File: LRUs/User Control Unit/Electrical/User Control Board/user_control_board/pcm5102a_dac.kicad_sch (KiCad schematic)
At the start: 1 part, among them U2 PCM5102A

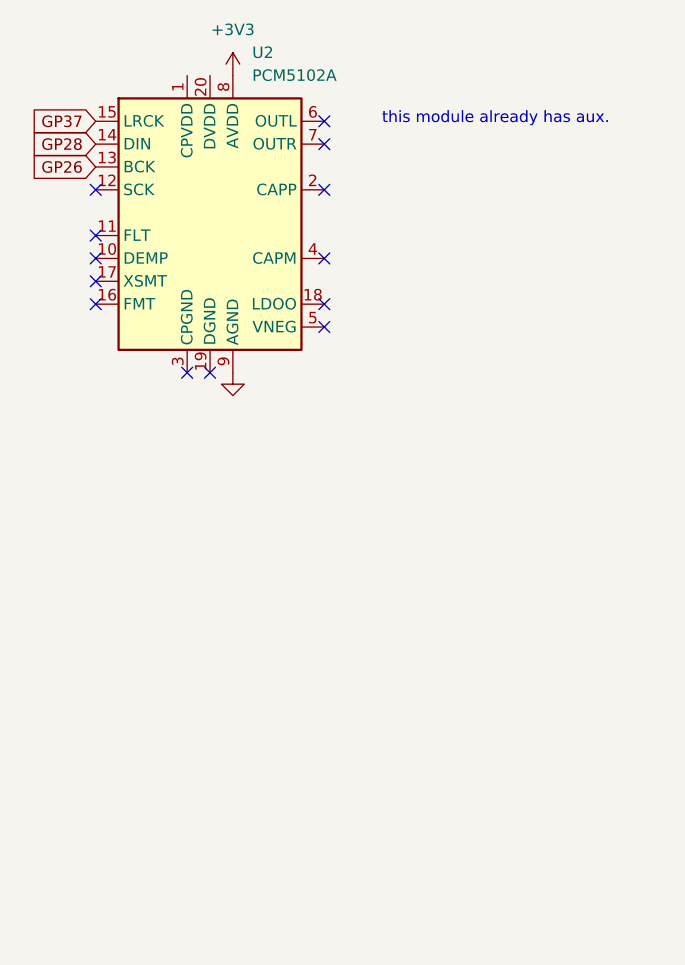
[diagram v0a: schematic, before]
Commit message: footprint and added symbol for audio
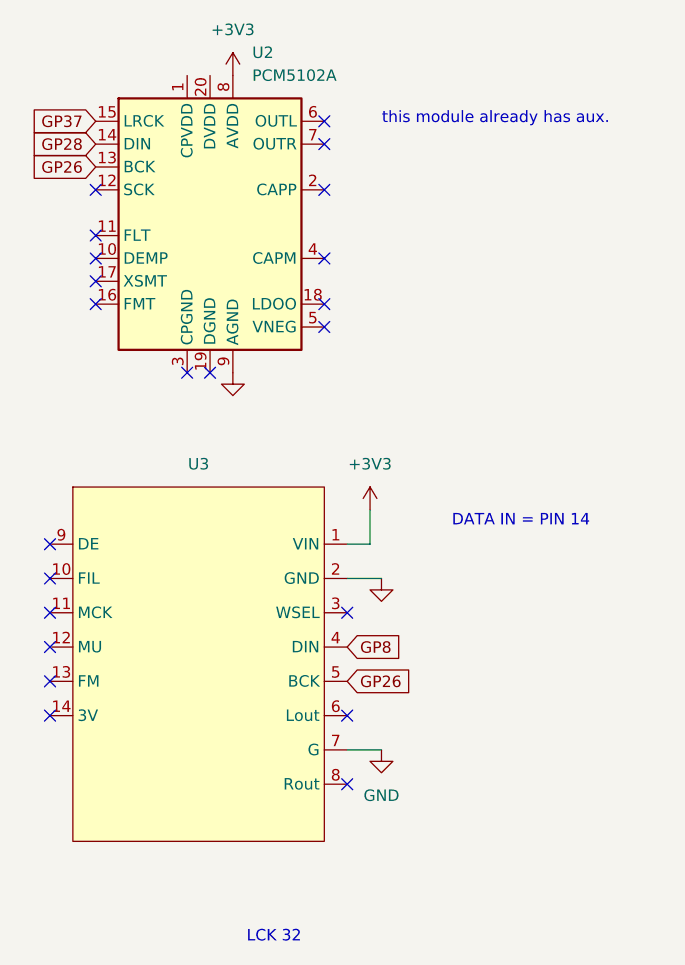
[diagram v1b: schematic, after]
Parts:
- added U3: (no value), symbol symbols:PCM5102
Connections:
- net +3V3: now also U3.1 (VIN)
- net GND: now also U3.2 (GND), U3.7 (G)
- net GP26: now also U3.5 (BCK)
- new net GP8: U3.4 (DIN)
- no-connect marks 13 -> 22
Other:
- note added: "DATA IN = PIN 14"
- note added: "LCK 32"

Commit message: drc run
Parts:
- removed U2: PCM5102A, Package_SO:TSSOP-20_4.4x6.5mm_P0.65mm, symbol Audio:PCM5102A
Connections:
- no-connect marks 22 -> 9
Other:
- note removed: "this module already has aux."

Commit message: need to run DCR
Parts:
- U3: footprint (none) -> footprints:Adafruit PCM510x I2S DAC
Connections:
- net GP27: now reaches U3.3 (WSEL)
- net GP8 renamed GP28
- no-connect marks 9 -> 8
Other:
- note added: "LCK?"
- note removed: "DATA IN = PIN 14"
- note removed: "LCK 32"
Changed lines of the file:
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@@
 	(generator_version "10.0")
 	(paper "A4")
-	(text "DATA IN = PIN 14\n"
-		(exclude_from_sim no)
-		(at 139.954 125.73 0)
+	(text "LCK?"
+		(exclude_from_sim no)
+		(at 132.08 136.144 0)
 		(effects
 			(font
@@
 		)
 	)
-	(text "LCK 32\n"
-		(exclude_from_sim no)
-		(at 112.522 171.958 0)
+	(text ""
+		(exclude_from_sim no)
+		(at 135.636 143.764 0)
 		(effects
 			(font
@@
 	)
 	(no_connect
-		(at 120.65 135.89)
-	)
-	(no_connect
 		(at 87.63 143.51)
 	)
@@
 		)
 	)
-	(global_label "GP8"
-		(shape input)
-		(at 120.65 139.7 0)
+	(global_label "GP27"
+		(shape output)
+		(at 120.65 135.89 0)
 		(fields_autoplaced yes)
 		(effects
@@
 		)
 		(property "Intersheetrefs" "${INTERSHEET_REFS}"
-			(at 127.3847 139.7 0)
+			(at 128.5942 135.89 0)
 			(hide yes)
 			(show_name no)
@@
 		)
 	)
+	(global_label "GP28"
+		(shape output)
+		(at 120.65 139.7 0)
+		(fields_autoplaced yes)
+		(effects
+			(font
+				(size 1.27 1.27)
+			)
+			(justify left)
+		)
+		(property "Intersheetrefs" "${INTERSHEET_REFS}"
+			(at 128.5942 139.7 0)
+			(hide yes)
+			(show_name no)
+			(do_not_autoplace no)
+			(effects
+				(font
+					(size 1.27 1.27)
+				)
+				(justify left)
+			)
+		)
+	)
 	(global_label "GP26"
-		(shape input)
+		(shape output)
 		(at 120.65 143.51 0)
 		(fields_autoplaced yes)
@@
 			)
 		)
-		(property "Footprint" ""
+		(property "Footprint" "footprints:Adafruit PCM510x I2S DAC"
 			(at 102.87 148.59 0)
 			(hide yes)

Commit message: connectors and 5v buck partially done
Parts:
- renumbered U3 to U5
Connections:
- net GP26 renamed DAC_BCK
- net GP27 renamed DAC_WSEL
- net GP28 renamed DAC_DIN
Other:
- note removed: "LCK?"
- moved on the sheet: U5
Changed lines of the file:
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@@
 	(generator_version "10.0")
 	(paper "A4")
-	(text "LCK?"
+	(text ""
 		(exclude_from_sim no)
-		(at 132.08 136.144 0)
+		(at 159.766 104.394 0)
 		(effects
 			(font
@@
 		)
 	)
-	(text ""
-		(exclude_from_sim no)
-		(at 135.636 143.764 0)
+	(no_connect
+		(at 109.22 106.68)
+	)
+	(no_connect
+		(at 142.24 110.49)
+	)
+	(no_connect
+		(at 109.22 99.06)
+	)
+	(no_connect
+		(at 142.24 118.11)
+	)
+	(no_connect
+		(at 109.22 95.25)
+	)
+	(no_connect
+		(at 109.22 91.44)
+	)
+	(no_connect
+		(at 109.22 110.49)
+	)
+	(no_connect
+		(at 109.22 102.87)
+	)
+	(wire
+		(pts
+			(xy 144.78 91.44) (xy 142.24 91.44)
+		)
+		(stroke
+			(width 0)
+			(type default)
+		)
+	)
+	(wire
+		(pts
+			(xy 142.24 114.3) (xy 146.05 114.3)
+		)
+		(stroke
+			(width 0)
+			(type default)
+		)
+	)
+	(wire
+		(pts
+			(xy 142.24 95.25) (xy 151.13 95.25)
+		)
+		(stroke
+			(width 0)
+			(type default)
+		)
+	)
+	(wire
+		(pts
+			(xy 144.78 87.63) (xy 144.78 91.44)
+		)
+		(stroke
+			(width 0)
+			(type default)
+		)
+	)
+	(global_label "DAC_WSEL"
+		(shape output)
+		(at 142.24 99.06 0)
+		(fields_autoplaced yes)
 		(effects
 			(font
 				(size 1.27 1.27)
 			)
-		)
-	)
-	(no_connect
-		(at 87.63 143.51)
-	)
-	(no_connect
-		(at 120.65 147.32)
-	)
-	(no_connect
-		(at 87.63 135.89)
-	)
-	(no_connect
-		(at 120.65 154.94)
-	)
-	(no_connect
-		(at 87.63 132.08)
-	)
-	(no_connect
-		(at 87.63 128.27)
-	)
-	(no_connect
-		(at 87.63 147.32)
-	)
-	(no_connect
-		(at 87.63 139.7)
-	)
-	(wire
-		(pts
-			(xy 123.19 128.27) (xy 120.65 128.27)
-		)
-		(stroke
-			(width 0)
-			(type default)
-		)
-	)
-	(wire
-		(pts
-			(xy 120.65 151.13) (xy 124.46 151.13)
-		)
-		(stroke
-			(width 0)
-			(type default)
-		)
-	)
-	(wire
-		(pts
-			(xy 120.65 132.08) (xy 124.46 132.08)
-		)
-		(stroke
-			(width 0)
-			(type default)
-		)
-	)
-	(wire
-		(pts
-			(xy 123.19 124.46) (xy 123.19 128.27)
-		)
-		(stroke
-			(width 0)
-			(type default)
-		)
-	)
-	(global_label "GP27"
+			(justify left)
+		)
+		(property "Intersheetrefs" "${INTERSHEET_REFS}"
+			(at 154.6594 99.06 0)
+			(hide yes)
+			(show_name no)
+			(do_not_autoplace no)
+			(effects
+				(font
+					(size 1.27 1.27)
+				)
+				(justify left)
+			)
+		)
+	)
+	(global_label "DAC_DIN"
 		(shape output)
-		(at 120.65 135.89 0)
+		(at 142.24 102.87 0)
 		(fields_autoplaced yes)
 		(effects
@@
 		)
 		(property "Intersheetrefs" "${INTERSHEET_REFS}"
-			(at 128.5942 135.89 0)
+			(at 153.0267 102.87 0)
 			(hide yes)
 			(show_name no)
@@
 		)
 	)
-	(global_label "GP28"
-		(shape output)
-		(at 120.65 139.7 0)
+	(global_label "DAC_BCK"
+		(shape input)
+		(at 142.24 106.68 0)
 		(fields_autoplaced yes)
 		(effects
@@
 		)
 		(property "Intersheetrefs" "${INTERSHEET_REFS}"
-			(at 128.5942 139.7 0)
-			(hide yes)
-			(show_name no)
-			(do_not_autoplace no)
-			(effects
-				(font
-					(size 1.27 1.27)
-				)
-				(justify left)
-			)
-		)
-	)
-	(global_label "GP26"
-		(shape output)
-		(at 120.65 143.51 0)
-		(fields_autoplaced yes)
-		(effects
-			(font
-				(size 1.27 1.27)
-			)
-			(justify left)
-		)
-		(property "Intersheetrefs" "${INTERSHEET_REFS}"
-			(at 128.5942 143.51 0)
+			(at 153.6314 106.68 0)
 			(hide yes)
 			(show_name no)
@@
 	(symbol
 		(lib_id "power:GND")
-		(at 124.46 151.13 0)
+		(at 146.05 114.3 0)
 		(unit 1)
 		(body_style 1)
@@
 		(dnp no)
 		(fields_autoplaced yes)
-		(property "Reference" "#PWR021"
-			(at 124.46 157.48 0)
+		(property "Reference" "#PWR059"
+			(at 146.05 120.65 0)
 			(hide yes)
 			(show_name no)
@@
 		)
 		(property "Value" "GND"
-			(at 124.46 156.21 0)
+			(at 146.05 119.38 0)
 			(show_name no)
 			(do_not_autoplace no)
@@
 		)
 		(property "Footprint" ""
-			(at 124.46 151.13 0)
+			(at 146.05 114.3 0)
 			(hide yes)
 			(show_name no)
@@
 		)
 		(property "Datasheet" ""
-			(at 124.46 151.13 0)
+			(at 146.05 114.3 0)
 			(hide yes)
 			(show_name no)
@@
 		)
 		(property "Description" "Power symbol creates a global label with name \"GND\" , ground"
-			(at 124.46 151.13 0)
+			(at 146.05 114.3 0)
 			(hide yes)
 			(show_name no)
@@
 			(project "user_control_board"
 				(path "/a075224b-ddb1-4e5b-b4ec-df1a39dc2291"
-					(reference "#PWR021")
+					(reference "#PWR059")
 					(unit 1)
 				)
@@
 	(symbol
 		(lib_id "power:GND")
-		(at 124.46 132.08 0)
+		(at 151.13 95.25 0)
 		(unit 1)
 		(body_style 1)
@@
 		(dnp no)
 		(fields_autoplaced yes)
-		(property "Reference" "#PWR020"
-			(at 124.46 138.43 0)
+		(property "Reference" "#PWR058"
+			(at 151.13 101.6 0)
 			(hide yes)
 			(show_name no)
@@
 		)
 		(property "Value" "GND"
-			(at 124.46 137.16 0)
+			(at 151.13 100.33 0)
 			(hide yes)
 			(show_name no)
@@
 		)
 		(property "Footprint" ""
-			(at 124.46 132.08 0)
+			(at 151.13 95.25 0)
 			(hide yes)
 			(show_name no)
@@
 		)
 		(property "Datasheet" ""
-			(at 124.46 132.08 0)
+			(at 151.13 95.25 0)
 			(hide yes)
 			(show_name no)
@@
 		)
 		(property "Description" "Power symbol creates a global label with name \"GND\" , ground"
-			(at 124.46 132.08 0)
+			(at 151.13 95.25 0)
 			(hide yes)
 			(show_name no)
@@
 			(project "user_control_board"
 				(path "/a075224b-ddb1-4e5b-b4ec-df1a39dc2291"
-					(reference "#PWR020")
+					(reference "#PWR058")
 					(unit 1)
 				)
@@
 	(symbol
 		(lib_id "power:+3V3")
-		(at 123.19 124.46 0)
+		(at 144.78 87.63 0)
 		(unit 1)
 		(body_style 1)
@@
 		(dnp no)
 		(fields_autoplaced yes)
-		(property "Reference" "#PWR019"
-			(at 123.19 128.27 0)
+		(property "Reference" "#PWR057"
+			(at 144.78 91.44 0)
 			(hide yes)
 			(show_name no)
@@
 		)
 		(property "Value" "+3V3"
-			(at 123.19 119.38 0)
+			(at 144.78 82.55 0)
 			(show_name no)
 			(do_not_autoplace no)
@@
 		)
 		(property "Footprint" ""
-			(at 123.19 124.46 0)
+			(at 144.78 87.63 0)
 			(hide yes)
 			(show_name no)
@@
 		)
 		(property "Datasheet" ""
-			(at 123.19 124.46 0)
+			(at 144.78 87.63 0)
 			(hide yes)
 			(show_name no)
@@
 		)
 		(property "Description" "Power symbol creates a global label with name \"+3V3\""
-			(at 123.19 124.46 0)
+			(at 144.78 87.63 0)
 			(hide yes)
 			(show_name no)
@@
 			(project "user_control_board"
 				(path "/a075224b-ddb1-4e5b-b4ec-df1a39dc2291"
-					(reference "#PWR019")
+					(reference "#PWR057")
 					(unit 1)
 				)
@@
 	(symbol
 		(lib_id "symbols:PCM5102")
-		(at 102.87 148.59 0)
+		(at 127 109.22 0)
 		(unit 1)
 		(body_style 1)
@@
 		(dnp no)
 		(fields_autoplaced yes)
-		(property "Reference" "U3"
-			(at 104.14 119.38 0)
+		(property "Reference" "U5"
+			(at 128.27 80.01 0)
 			(show_name no)
 			(do_not_autoplace no)
@@
 		)
 		(property "Value" ""
-			(at 102.87 148.59 0)
+			(at 127 109.22 0)
 			(show_name no)
 			(do_not_autoplace no)
@@
 		)
 		(property "Footprint" "footprints:Adafruit PCM510x I2S DAC"
-			(at 102.87 148.59 0)
+			(at 127 109.22 0)
 			(hide yes)
 			(show_name no)
@@
 		)
 		(property "Datasheet" ""
-			(at 102.87 148.59 0)
+			(at 127 109.22 0)
 			(hide yes)
 			(show_name no)
@@
 		)
 		(property "Description" ""
-			(at 102.87 148.59 0)
+			(at 127 109.22 0)
 			(hide yes)
 			(show_name no)
@@
 			(project "user_control_board"
 				(path "/a075224b-ddb1-4e5b-b4ec-df1a39dc2291"
-					(reference "U3")
+					(reference "U5")
 					(unit 1)
 				)
